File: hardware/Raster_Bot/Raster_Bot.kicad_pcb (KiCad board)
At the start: 4 copper layers, 65 x 28 mm, 68 parts, among them J1 JST_PH, J2 USB_C_Receptacle_USB2.0_16P, J3 Conn_EYESPI, J4 Conn_Motor_N20_Encoder, J5 Conn_Motor_N20_Encoder, Q1 AO3401A, Q2 2N7002, Q3 AO3401A, SW1 SW_RESET, SW2 SW_BOOT, SW3 SW_SPDT_SH, U1 ESP32-S3-MINI-1, U2 BQ24072RGT, U3 DRV8833PWPR, U4 AP2114H-3.3, U5 TPS61023DRLR

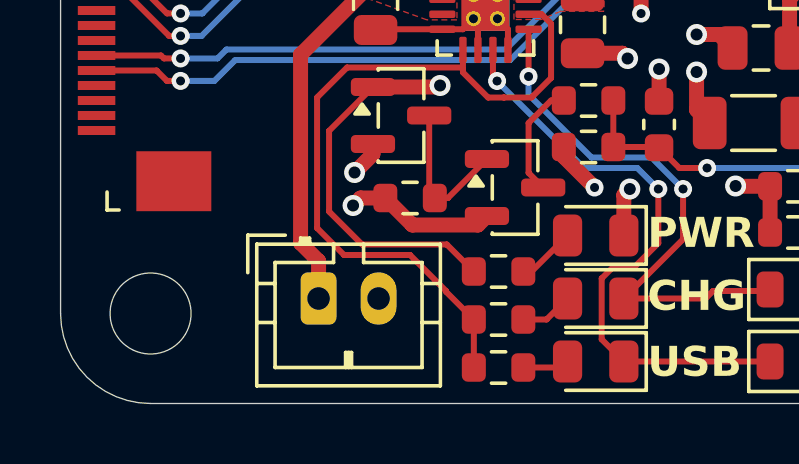
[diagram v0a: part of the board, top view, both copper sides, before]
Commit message: [hardware] Vendor 3D models locally and upgrade to KiCad 10
Co-authored-by: Cursor <cursoragent@cursor.com>
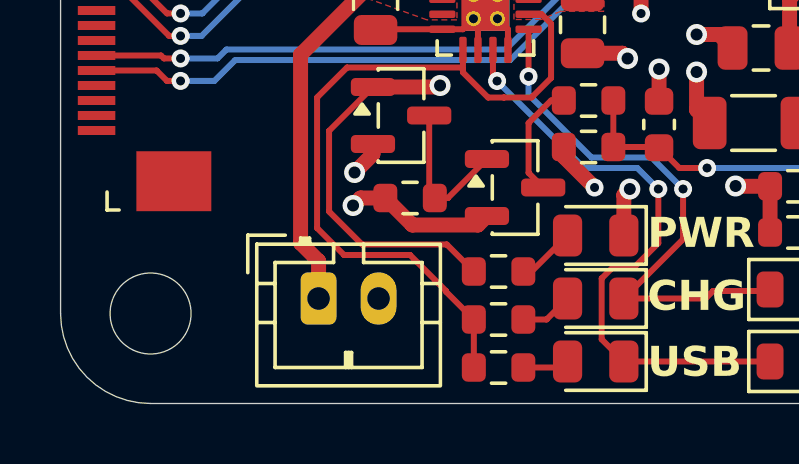
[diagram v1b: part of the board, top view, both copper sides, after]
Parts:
- L1: footprint Inductor_SMD:L_Coilcraft_XxL4030 -> Raster_Bot:L_Coilcraft_XxL4030
- SW3: footprint Button_Switch_SMD:SW_SPDT_Shouhan_MSK12C02 -> Raster_Bot:SW_SPDT_Shouhan_MSK12C02
